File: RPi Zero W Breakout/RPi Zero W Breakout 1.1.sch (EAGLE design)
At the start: 34 parts, among them J1 DX4R005HJ5R2000, J2 S2B-PH-SM4-TB(LF)(SN), T1 MMUN2133LT1G, U1 TPS61090RSAR, U2 MCP73871T-2CCI/ML

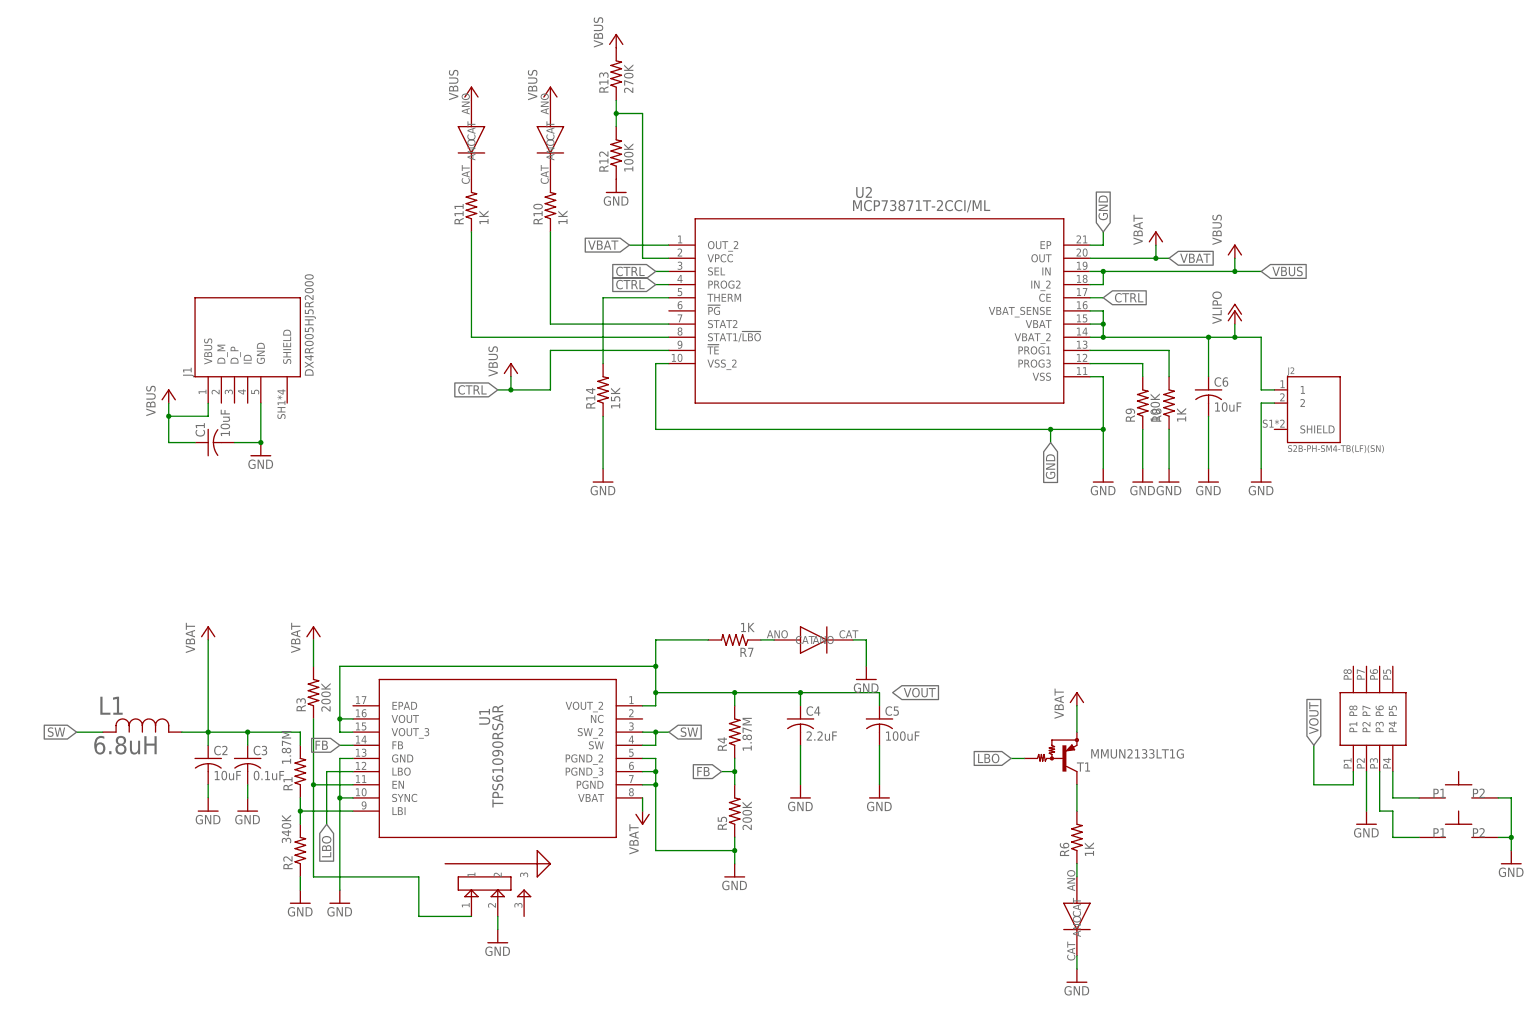
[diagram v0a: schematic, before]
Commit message: Update
Moved shoulder buttons to LiPoly Management and extended LiPoly Management's dimensions. After looking at the boards in Fusion 360, I decided it would be better to have the shoulder buttons lower, rather than up high on RPi Zero Breakout. Rereouted LiPoly due to this.
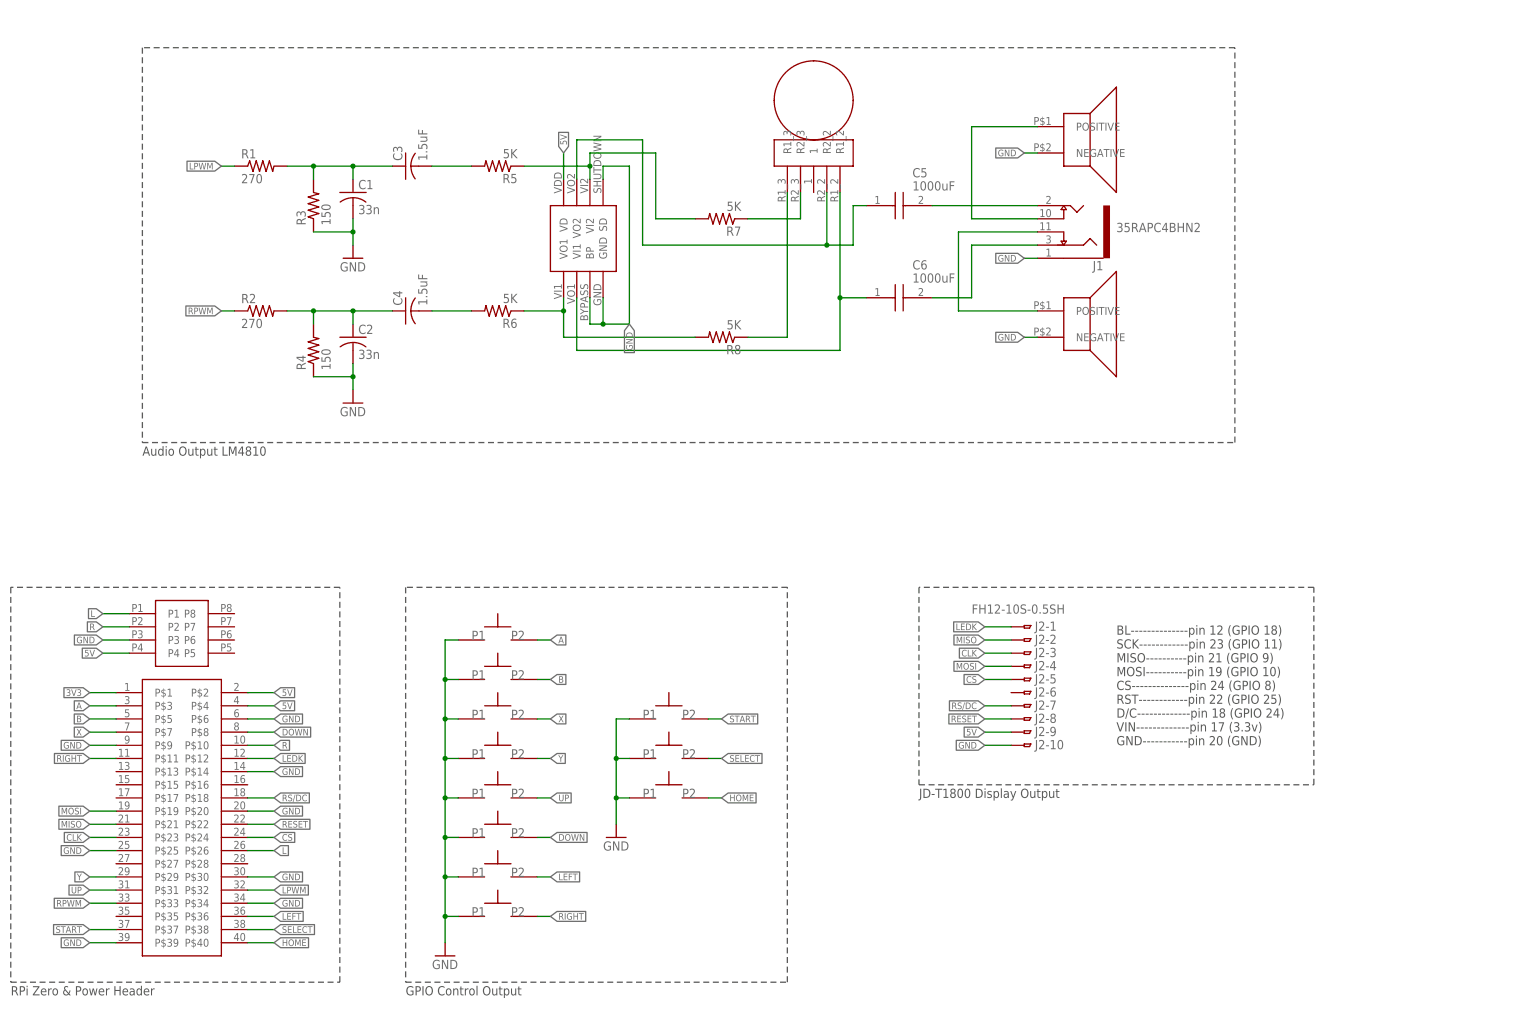
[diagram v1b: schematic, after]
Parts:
- removed CHARGE: YELLOW, KingBright:WP934AD
- removed DONE: GREEN, KingBright:WP934AD
- removed L1: 6.8uH, VLCF5020T-6R8N1R1:VLCF5020T
- removed LBO: RED, KingBright:WP934AD
- removed POWERON: BLUE, KingBright:WP934EW
- removed R10, R11: 1K, rcl:R-US_R0805
- removed R12, R9: 100K, rcl:R-US_R0805
- removed R13: 270K, rcl:R-US_R0805
- removed R14: 15K, rcl:R-US_R0805
- removed T1: MMUN2133LT1G, transistor:MUN2114T1-PNP_DRIVER-SC59-BEC
- removed U$3: SPST_TACTILE_SWITCHRIGHTANGLEBENT, switches:SPST_TACTILE_SWITCHRIGHTANGLEBENT
- removed U1: TPS61090RSAR, TPS61090RSAR:TPS61090RSAR
- removed U2: MCP73871T-2CCI/ML, MCP73871T-2CCI:MCP73871T-2CCI/ML
- added A, START: SPST_TACTILE_SWITCH, switches:SPST_TACTILE_SWITCH
- added B, DOWN, HOME, LEFT, RIGHT, SELECT, UP, X, Y: SPST_TACTILESWITCH_TL3301PF160QG, switches:SPST_TACTILESWITCH_TL3301PF160QG
- added LSPK, RSPK: SP-1208, SP-1208:SP-1208
- added RF: RK14J12A0A0K, RK14J12A0A0K:RK14J12A0A0K
- C1, C2: value 10uF -> 33n; device rcl:C-USC0805 -> rcl:C-USC0805K
- C3: value 0.1uF -> 1.5uF; device rcl:C-USC0805 -> rcl:C-USC0805K
- C4: value 2.2uF -> 1.5uF; device rcl:C-USC0805 -> rcl:C-USC0805K
- C5: value 100uF -> 1000uF; device rcl:C-USC0805 -> SamacSys_Parts:UWT0J102MNL1GS
- C6: value 10uF -> 1000uF; device rcl:C-USC0805 -> SamacSys_Parts:UWT0J102MNL1GS
- J1: value DX4R005HJ5R2000 -> 35RAPC4BHN2; device DX4R005HJ5R2000:DX4R005HJ5R2000 -> 35RAPC4BHN2:35RAPC4BHN2
- J2: value S2B-PH-SM4-TB(LF)(SN) -> FH12-10S-0.5SH; device S2B-PH-SM4-TB_LF__SN_:S2B-PH-SM4-TB(LF)(SN) -> con-hirose:FH12-10S-0.5SH
- R1: value 1.87M -> 270
- R2: value 340K -> 270
- R3: value 200K -> 150
- R4: value 1.87M -> 150
- R5: value 200K -> 5K
- R6, R7, R8: value 1K -> 5K
- U$1: value SPST_TACTILE_SWITCHRIGHTANGLEBENT -> RPI_ZERO; device switches:SPST_TACTILE_SWITCHRIGHTANGLEBENT -> RaspberryPi:RPI_ZERO
- U$2: value JS102011SAQN -> LM4810MM/NOPBCT-ND; device JS102011SAQN:JS102011SAQN -> LM4810MM:LM4810MM/NOPBCT-ND
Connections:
- removed net +3V3: CHARGE.ANO, DONE.ANO, R13.2
- removed net CTRL: U2.!TE, U2.CE, U2.PROG2, U2.SEL
- removed net FB: R4.1, R5.2, U1.FB
- removed net LBO: T1.B, U1.LBO
- removed net N$3: CHARGE.CAT, R11.2
- removed net SW: L1.2, U1.SW, U1.SW_2
- removed net VBAT: C2.1, C3.1, L1.1, R1.2, R3.2, T1.E, U1.VBAT, U2.OUT, U2.OUT_2
- removed net VBUS: C1.1, J1.VBUS, U2.IN, U2.IN_2
- removed net VLIPO: C6.1, J2.1, U2.VBAT, U2.VBAT_2, U2.VBAT_SENSE
- removed net VOUT: C4.1, C5.1, H1.P1, R4.2, R7.2, U1.VOUT, U1.VOUT_2, U1.VOUT_3
- new net 3V3: U$1.P$1
- new net 5V: H1.P4, J2-9.1, U$1.P$2, U$1.P$4, U$2.VD
- new net A: A.P$2, U$1.P$3
- new net B: B.P$2, U$1.P$5
- new net CLK: J2-3.1, U$1.P$23
- new net CS: J2-5.1, U$1.P$24
- new net DOWN: DOWN.P$2, U$1.P$8
- new net HOME: HOME.P$2, U$1.P$40
- new net L: H1.P1, U$1.P$26
- new net LEDK: J2-1.1, U$1.P$12
- new net LEFT: LEFT.P$2, U$1.P$36
- new net LPWM: R1.1, U$1.P$32
- new net MISO: J2-2.1, U$1.P$21
- new net MOSI: J2-4.1, U$1.P$19
- new net R: H1.P2, U$1.P$10
- new net RESET: J2-8.1, U$1.P$22
- new net RIGHT: RIGHT.P$2, U$1.P$11
- new net RPWM: R2.1, U$1.P$33
- new net RS/DC: J2-7.1, U$1.P$18
- new net SELECT: SELECT.P$2, U$1.P$38
- new net START: START.P$2, U$1.P$37
- new net UP: U$1.P$31, UP.P$2
- new net X: U$1.P$7, X.P$2
- new net Y: U$1.P$29, Y.P$2
- net GND: now also A.P$1, B.P$1, DOWN.P$1, H1.P3, HOME.P$1, J1.1, J2-10.1, LEFT.P$1, LSPK.NEGATIVE, R3.1, R4.1, RIGHT.P$1, RSPK.NEGATIVE, SELECT.P$1, START.P$1, U$1.P$14, U$1.P$20, U$1.P$25, U$1.P$30, U$1.P$34, U$1.P$39, U$1.P$6, U$1.P$9, U$2.BP, U$2.GND, U$2.SD, UP.P$1, X.P$1, Y.P$1; no longer C3.2, C4.2, C5.2, C6.2, H1.P2, J1.GND, J2.2, LBO.CAT, POWERON.CAT, R12.1, R14.1, R2.1, R5.1, R8.1, R9.1, U$1.P$2, U$2.2, U$3.P$2, U1.GND, U1.PGND, U1.PGND_2, U1.PGND_3, U1.SYNC, U2.EP, U2.VSS, U2.VSS_2
- net N$1: now also C1.1, C3.1, R1.2, R3.2; no longer R1.1, R2.2, U1.LBI
- net N$10: now also C5.-, J1.2; no longer H1.P4, U$1.P$1
- net N$11: now also C6.-, J1.3; no longer R11.1, U2.STAT1/!LBO
- net N$12: now also J1.10, LSPK.POSITIVE; no longer R10.1, U2.STAT2
- net N$13: now also J1.11, RSPK.POSITIVE; no longer R14.2, U2.THERM
- net N$14: now also R5.1, R7.2, U$2.VI2; no longer R12.2, R13.1, U2.VPCC
- net N$15: now also R6.1, R8.2, U$2.VO1; no longer H1.P3, U$3.P$1
- net N$2: now also C2.1, C4.1, R2.2, R4.2; no longer R3.1, U$2.1, U1.EN
- net N$4: now also C3.2, R5.2; no longer R8.2, U2.PROG1
- net N$5: now also R7.1, RF.R2_3; no longer R6.2, T1.C
- net N$6: now also C4.2, R6.2; no longer LBO.ANO, R6.1
- net N$7: now also R8.1, RF.R1_3; no longer POWERON.ANO, R7.1
- net N$8: now also C6.+, RF.R1_2, U$2.VI1; no longer R9.2, U2.PROG3
- net N$9: now also C5.+, RF.R2_2, U$2.VO2; no longer DONE.CAT, R10.2
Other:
- note added: "Audio Output LM4810"
- note added: "BL--------------pin 12 (GPIO 18) SCK------------pin 23 (GPIO 11) MISO----------pin 21 (GPIO 9) MOSI----------pin 19 (GPIO 10) CS--------------pin 24 (GPIO 8) RST------------pin 22 (GPIO 25) D/C-------------pin 18 (GPIO 24) VIN-------------pin 17 (3.3v) GND-----------pin 20 (GND)"
- note added: "GPIO Control Output"
- note added: "JD-T1800 Display Output"
- note added: "RPi Zero & Power Header"
- note removed: "A"
- note removed: "B"
- note removed: "Position A: EN is pulled to ground and VOUT is disabled Position B: EN floats and VOUT is enabled"
- moved on the sheet: C1, C2, C3, C4, R1, R2, R3, R4, R5, R6, R7, R8
